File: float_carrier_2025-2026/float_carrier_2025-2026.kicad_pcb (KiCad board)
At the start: 2 copper layers, 181.8 x 181.8 mm, 21 parts, among them J1 Conn_01x18_Socket, J2 Conn_01x18_Socket, J3 Screw_Terminal_01x04_Depth_Se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, J4 Screw_Terminal_01x03_Servo, J5 Screw_Terminal_01x03_GND, J6 Conn_01x07_Socket, J7 Screw_Terminal_01x02, U2 TPS563200

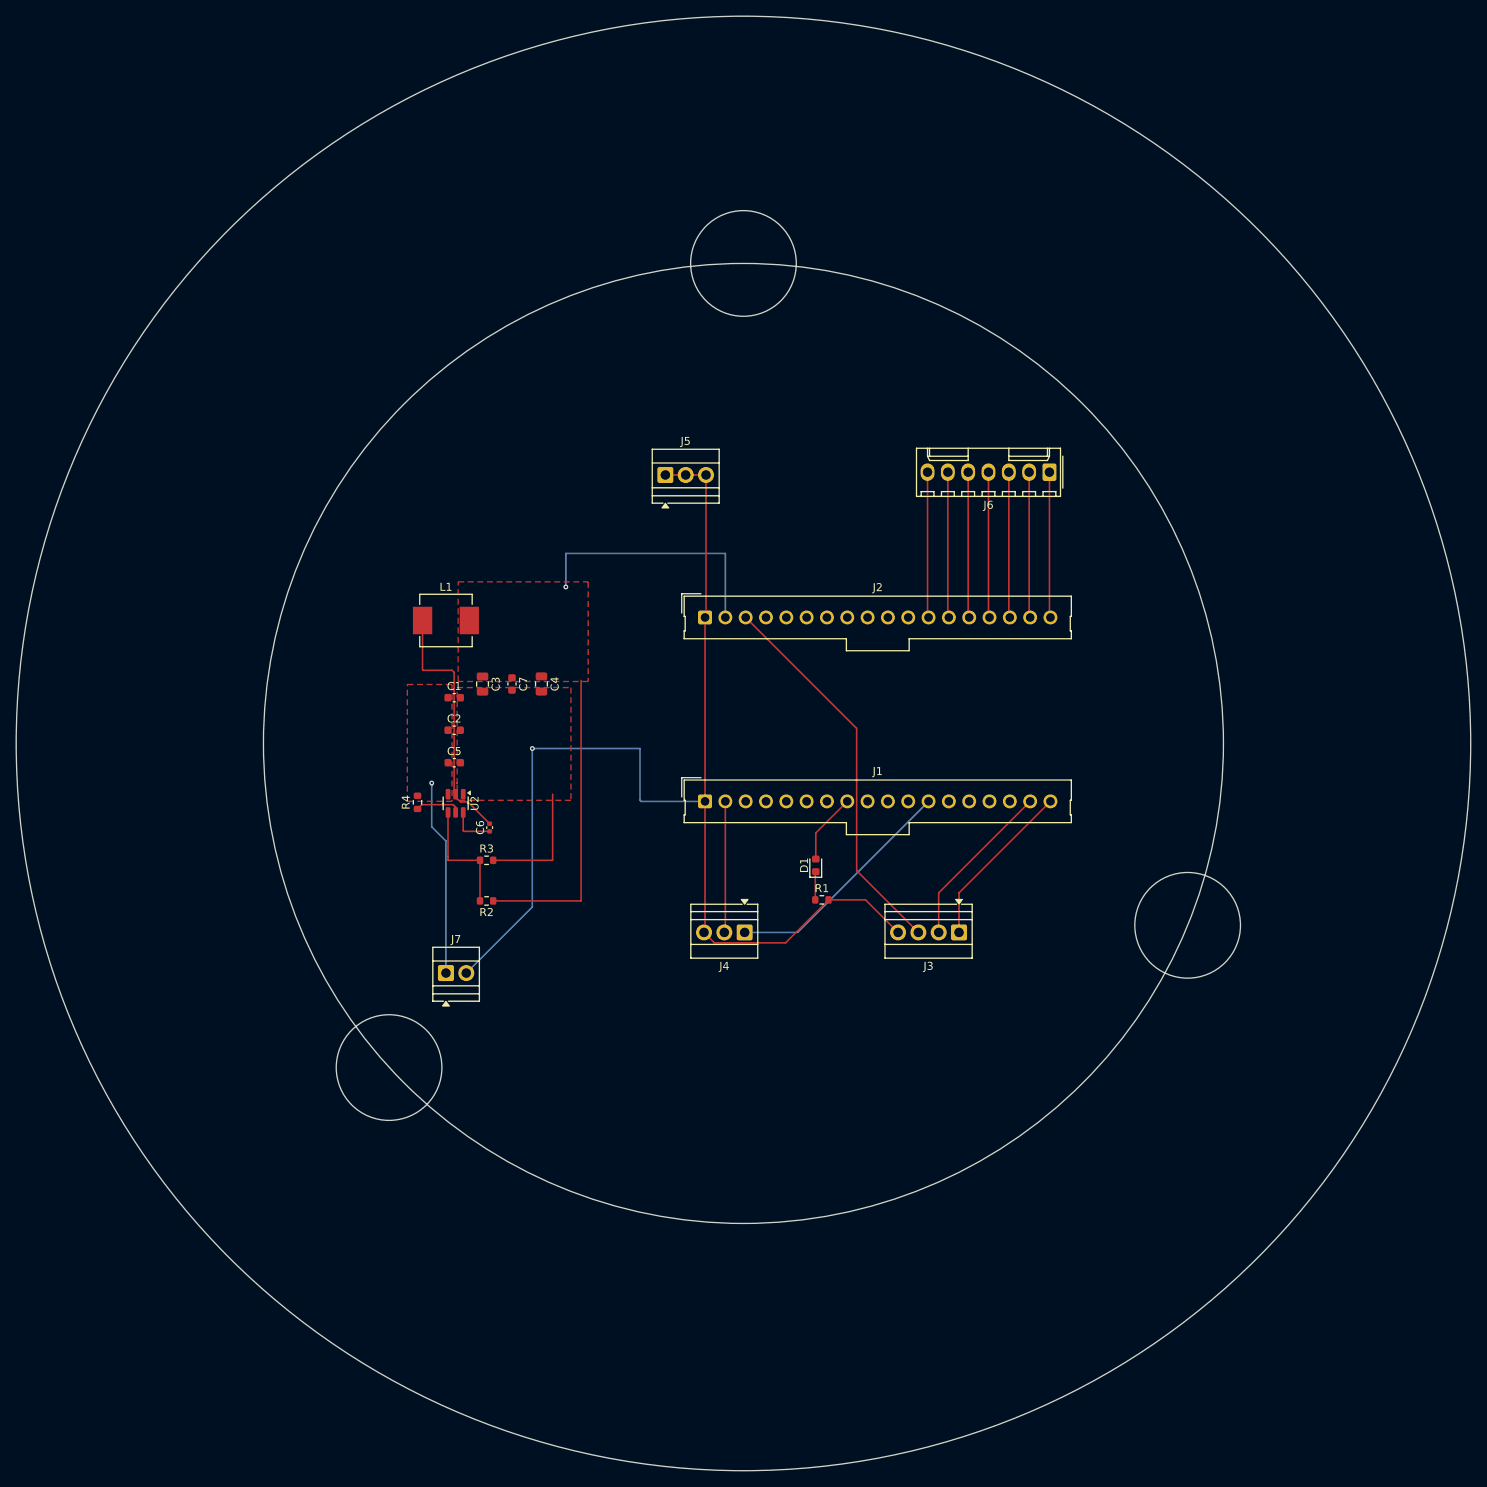
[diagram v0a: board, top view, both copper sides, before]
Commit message: Feat[float_carrier_2025-2026]:connectors 3D symbol fixed, edge cut fixed
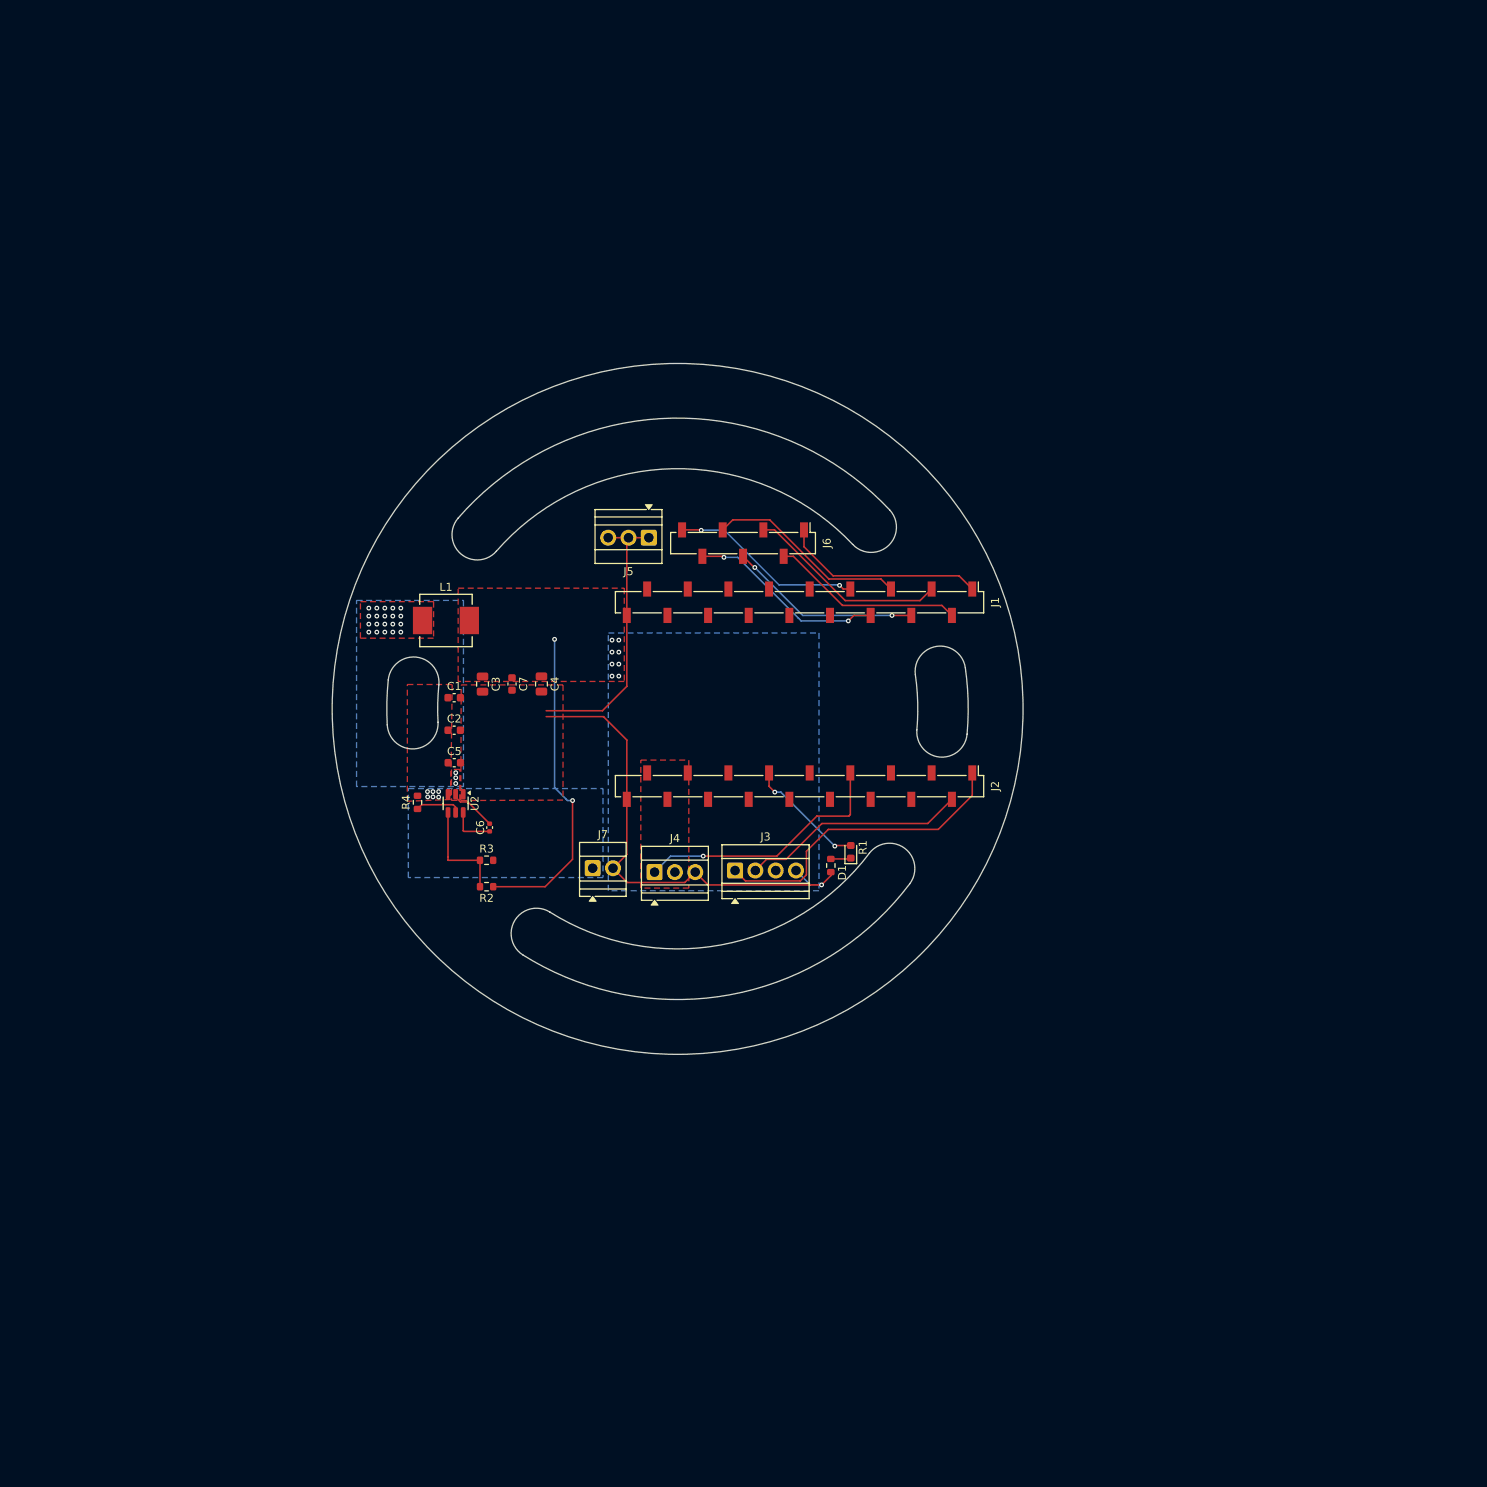
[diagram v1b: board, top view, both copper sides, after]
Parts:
- J1, J2: footprint Connector_Molex:Molex_SL_171971-0018_1x18_P2.54mm_Vertical -> Connector_PinSocket_2.54mm:PinSocket_1x18_P2.54mm_Vertical_SMD_Pin1Left
- J6: footprint Connector_Molex:Molex_KK-254_AE-6410-07A_1x07_P2.54mm_Vertical -> Connector_PinSocket_2.54mm:PinSocket_1x07_P2.54mm_Vertical_SMD_Pin1Left
- moved J6 39.3 mm to (109.8, 80.9), turned to -90 degrees
- moved J3 29.0 mm to (108.8, 121.8), turned to 0 degrees
- moved J1 27.6 mm to (116.8, 88.3), turned to -90 degrees
- moved J2 24.2 mm to (116.8, 111.3), turned to -90 degrees
- moved J7 22.5 mm to (91.0, 121.5)
- moved J4 13.6 mm to (98.7, 122.0), turned to 0 degrees
- moved J5 8.11 mm to (98.0, 80.2), turned to 180 degrees
- moved D1 4.70 mm to (123.2, 119.5)
- moved R1 4.44 mm to (120.8, 121.2), turned to -90 degrees
- moved R2 1.78 mm to (77.7, 123.8)
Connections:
- C1 pad 2: GNDREF -> GND
- C2 pad 2: GNDREF -> GND
- C5 pad 2: GNDREF -> GND
- J1 pad 1: GND -> /GPIO7
- J1 pad 10: /GPIO35 -> /GPIO40
- J1 pad 11: /GPIO34 -> /GPIO41
- J1 pad 12: /GPIO33 -> /GPIO42
- J1 pad 13: /GPIO47 -> /GPIO45
- J1 pad 14: /GPIO48 -> /GPIO46
- J1 pad 15: /GPIO26 -> /GPIO37
- J1 pad 16: /GPIO21 -> /3.3V
- J1 pad 17: /GPIO20/SCA -> /3.3V
- J1 pad 18: /GPIO19/SCL -> GND
- J1 pad 2: /5V -> /GPIO6
- J1 pad 3: /Ve -> /GPIO5
- J1 pad 4: /Ve -> /GPIO4
- J1 pad 5: /U0RXD/GPIO44 -> /GPIO3
- J1 pad 6: /U0TXD/GPIO43 -> /GPIO2
- J1 pad 7: /RST -> /GPIO1
- J1 pad 8: /GPIO0 -> /GPIO38
- J1 pad 9: /GPIO36 -> /GPIO39
- J2 pad 1: GND -> /GPIO19/SCL
- J2 pad 10: /GPIO39 -> /GPIO36
- J2 pad 11: /GPIO38 -> /GPIO0
- J2 pad 12: /GPIO1 -> /RST
- J2 pad 13: /GPIO2 -> /U0TXD/GPIO43
- J2 pad 14: /GPIO3 -> /U0RXD/GPIO44
- J2 pad 15: /GPIO4 -> /Ve
- J2 pad 16: /GPIO5 -> /Ve
- J2 pad 17: /GPIO6 -> /5V
- J2 pad 18: /GPIO7 -> GND
- J2 pad 2: /3.3V -> /GPIO20/SCA
- J2 pad 3: /3.3V -> /GPIO21
- J2 pad 4: /GPIO37 -> /GPIO26
- J2 pad 5: /GPIO46 -> /GPIO48
- J2 pad 6: /GPIO45 -> /GPIO47
- J2 pad 7: /GPIO42 -> /GPIO33
- J2 pad 8: /GPIO41 -> /GPIO34
- J2 pad 9: /GPIO40 -> /GPIO35
- U2 pad 1: GNDREF -> GND
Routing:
- net /3.3V: track 119.0 -> 40.1 mm, vias 1 -> 10
- net GND: track 166.2 -> 97.4 mm
- net Net-(U2-SW): track 31.9 -> 6.72 mm, vias 0 -> 23
- net /6V: track 24.9 -> 0.00 mm, vias 1 -> 6
- net /GPIO19/SCL: track 21.1 -> 39.1 mm
- net /5V: track 16.4 -> 0.00 mm
- net /GPIO20/SCA: track 21.1 -> 28.3 mm
- net /GPIO7: track 18.2 -> 25.3 mm
- net /GPIO5: track 18.2 -> 25.3 mm
- net /GPIO3: track 18.2 -> 25.1 mm
- net /GPIO2: track 18.2 -> 24.7 mm, vias 0 -> 2
- net /GPIO0: track 8.83 -> 15.0 mm, vias 0 -> 2
- net /GPIO4: track 18.2 -> 24.1 mm, vias 0 -> 2
- net /GPIO6: track 18.2 -> 24.1 mm
- net /GPIO1: track 18.2 -> 24.1 mm, vias 0 -> 2
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- added copper zone on B.Cu, net /3.3V
- added copper zone on F.Cu, net /5V
- added copper zone on B.Cu, net /6V
- added copper zone on B.Cu, net Net-(U2-SW)
- added copper zone on F.Cu, net Net-(U2-SW)
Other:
- board size 181.8 x 181.8 mm -> 86.4 x 86.4 mm

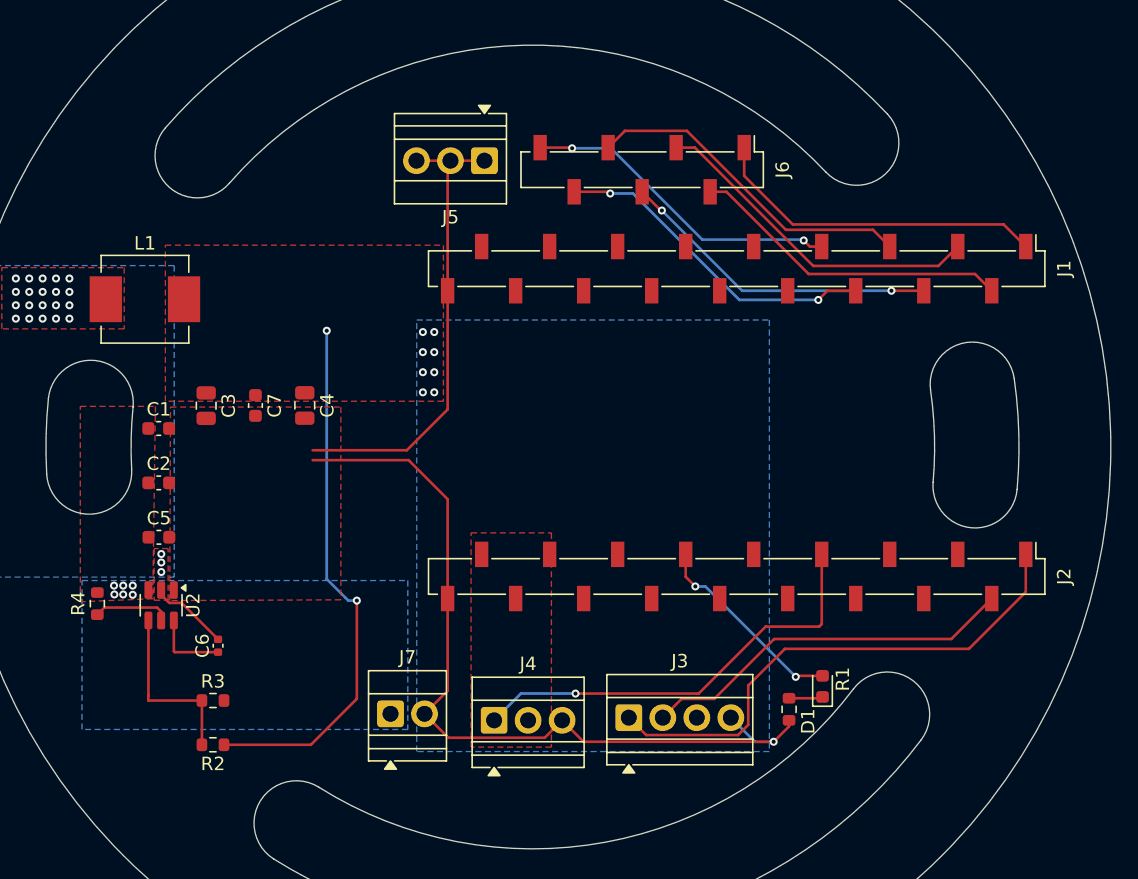
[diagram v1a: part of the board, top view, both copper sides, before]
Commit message: Feat[float_carrier_2025-2026]: silkscreen added, connectors and inductor changed, gerber file and BOM file made
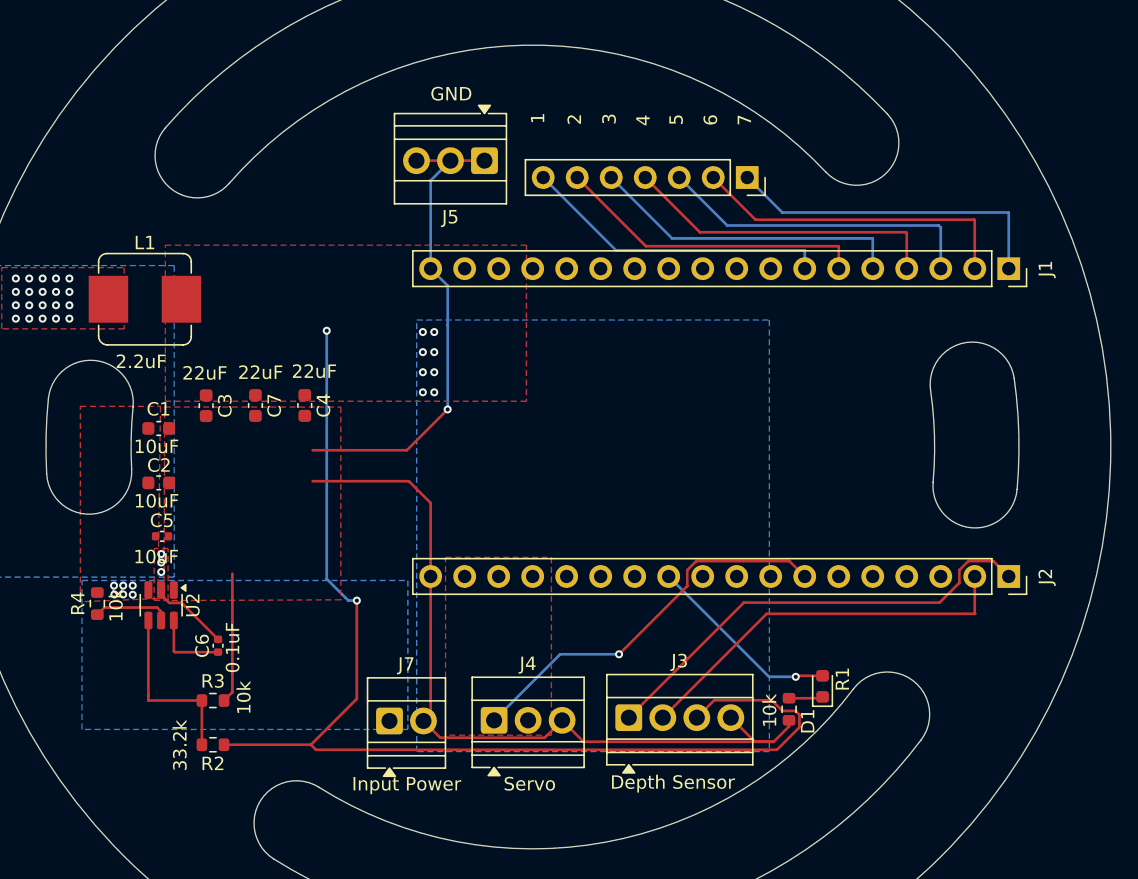
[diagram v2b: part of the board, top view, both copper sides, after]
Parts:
- C3, C4: footprint Capacitor_SMD:C_0805_2012Metric -> Capacitor_SMD:C_0603_1608Metric
- C5: footprint Capacitor_SMD:C_0603_1608Metric -> Capacitor_SMD:C_0402_1005Metric
- J1, J2: footprint Connector_PinSocket_2.54mm:PinSocket_1x18_P2.54mm_Vertical_SMD_Pin1Left -> Connector_PinSocket_2.54mm:PinSocket_1x18_P2.54mm_Vertical
- J6: footprint Connector_PinSocket_2.54mm:PinSocket_1x07_P2.54mm_Vertical_SMD_Pin1Left -> Connector_PinSocket_2.54mm:PinSocket_1x07_P2.54mm_Vertical
- L1: footprint Inductor_SMD:L_Vishay_IHLP-2525 -> Inductor_SMD:L_Bourns_SRP7028A_7.3x6.6mm
- moved J1 20.3 mm to (137.2, 88.3)
- moved J2 20.3 mm to (137.2, 111.3)
- moved J6 7.87 mm to (117.6, 81.5)
- moved J7 0.54 mm to (90.9, 122.0)
- moved C5 0.24 mm to (73.9, 108.3)
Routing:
- net /3.3V: track 40.1 -> 87.1 mm
- net GND: track 97.4 -> 106.3 mm
- net /GPIO19/SCL: track 39.1 -> 34.3 mm
- net /GPIO33: track 32.7 -> 29.3 mm
- net /GPIO3: track 25.1 -> 23.7 mm
- net /GPIO2: track 24.7 -> 23.3 mm, vias 2 -> 0
- net /GPIO5: track 25.3 -> 24.2 mm
- net /GPIO20/SCA: track 28.3 -> 29.3 mm
- net /GPIO1: track 24.1 -> 23.2 mm, vias 2 -> 0
- net /GPIO7: track 25.3 -> 24.8 mm
- net /GPIO0: track 15.0 -> 14.6 mm, vias 2 -> 1
- net /GPIO4: track 24.1 -> 23.9 mm, vias 2 -> 0
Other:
- board text added: "0.1uF"
- board text added: "1"
- board text added: "10k"
- board text added: "10uF"
- board text added: "2"
- board text added: "2.2uF"
- board text added: "22uF"
- board text added: "3"
- board text added: "33.2k"
- board text added: "4"
- board text added: "5"
- board text added: "6"
- board text added: "7"
- board text added: "Depth Sensor"
- board text added: "GND"
- board text added: "Input Power"
- board text added: "Servo"
